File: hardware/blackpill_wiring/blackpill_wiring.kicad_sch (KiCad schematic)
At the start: 7 parts, among them J1 ST7789_DISPLAY, J2 HOBBY_SERVO, J3 CRSF_RECEIVER, J4 BRUSHLESS_ESC, J5 ESP01_WIFI, J6 USB_HOST, U1 BLACKPILL_F411CE

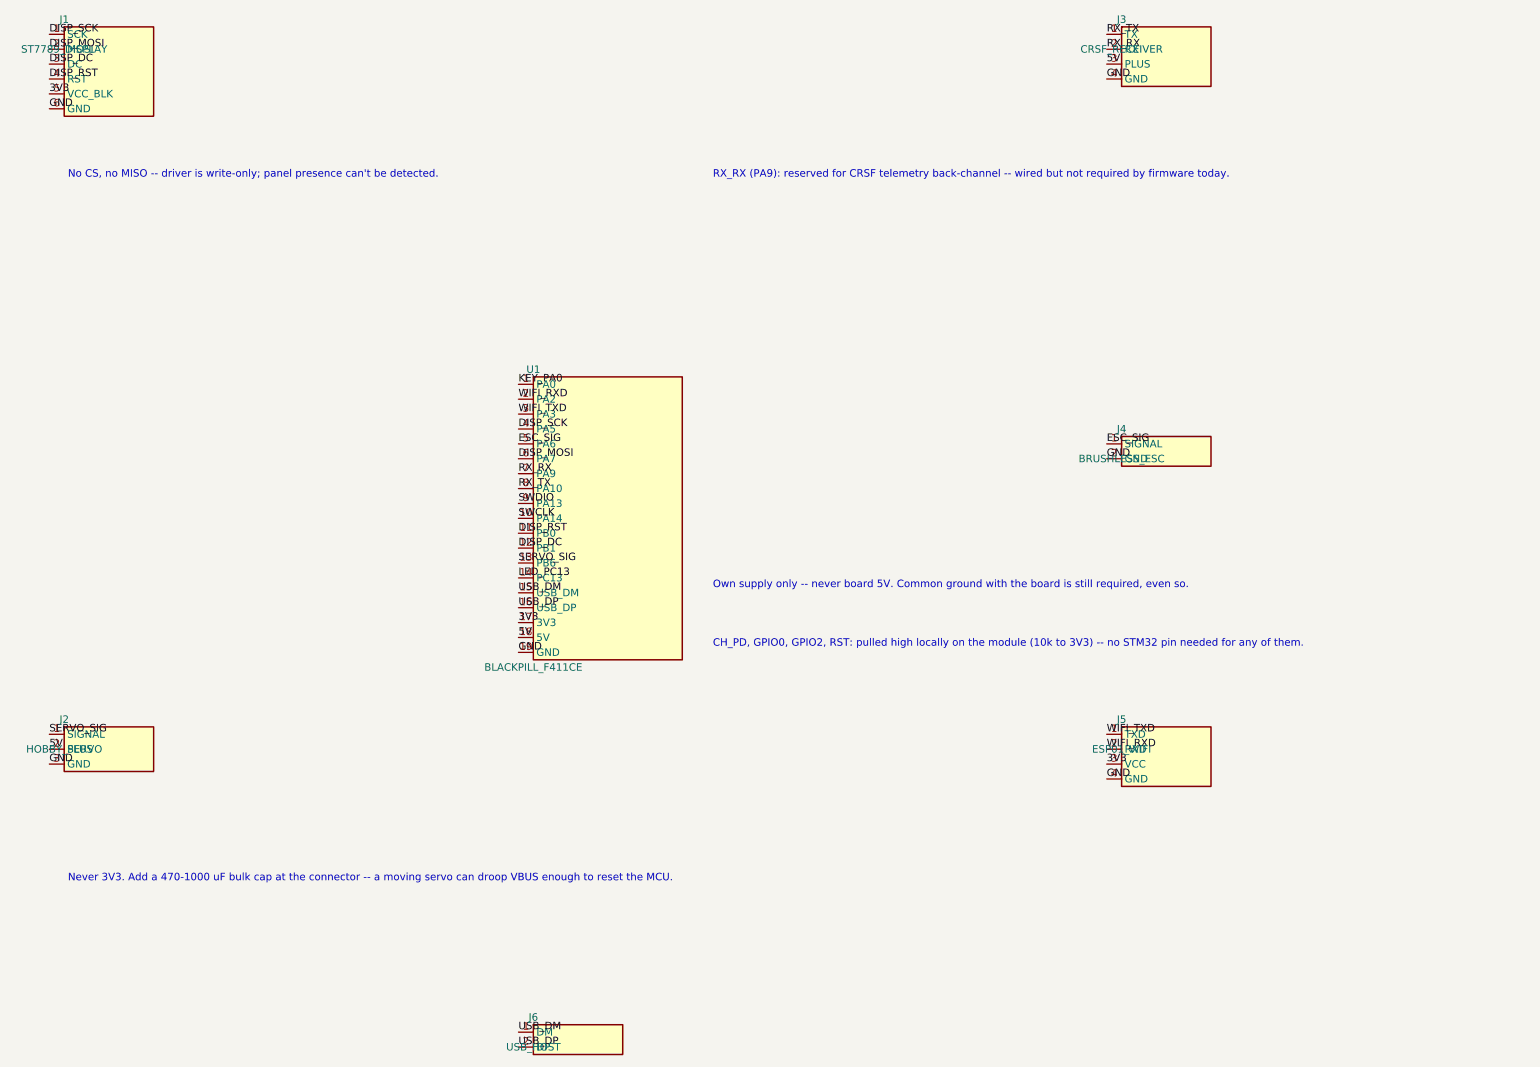
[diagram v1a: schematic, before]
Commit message: fix(hardware): draw real wires instead of net labels
Net labels were electrically correct (ERC-clean, all connections
verified) but visually unreadable as a wiring diagram: opening the
project showed components with no visible connection between them.
Reworked the schematic so every connection is an actual routed wire:

- BLACKPILL_F411CE now has pins split left/right (display+servo+USB
  on the left, receiver+ESC+WiFi on the right), matching the original
  SVG's own left/right stub grouping.
- ST7789_DISPLAY, HOBBY_SERVO and USB_HOST got their pins flipped to
  the right edge (facing the Black Pill, which sits to their right);
  CRSF_RECEIVER, BRUSHLESS_ESC and ESP01_WIFI keep their original
  left-facing pins (Black Pill sits to their right already).
- Every module's local pin Y-offsets are designed to exactly match
  the Black Pill's corresponding pin, then placed at the same sheet Y
  -- every wire is a straight 2-point horizontal line, no waypoint
  routing, no crossing over component bodies.
- Dropped PC13/PA0/PA13/PA14 as symbol pins entirely; the source SVG
  draws these as plain text badges, not wired stubs, so they're now
  add_schematic_text notes near U1 instead. Removes the 4 "label
  connected to only one pin" ERC notices from the previous version.

Verified against real KiCad 10.0.5 directly (not just the MCP
server's own tools, one of which -- list_schematic_nets -- turned out
to give a false "no nets found" on this file): `kicad-cli sch export
netlist` shows all 21 point-to-point nets correctly connected, and
`kicad-cli sch erc` reports 0 errors / 21 warnings, all either the
harmless lib_symbol_mismatch cache nag seen before or a cosmetic
endpoint_off_grid notice that doesn't affect actual connectivity.

Co-Authored-By: Claude Sonnet 5 <noreply@anthropic.com>
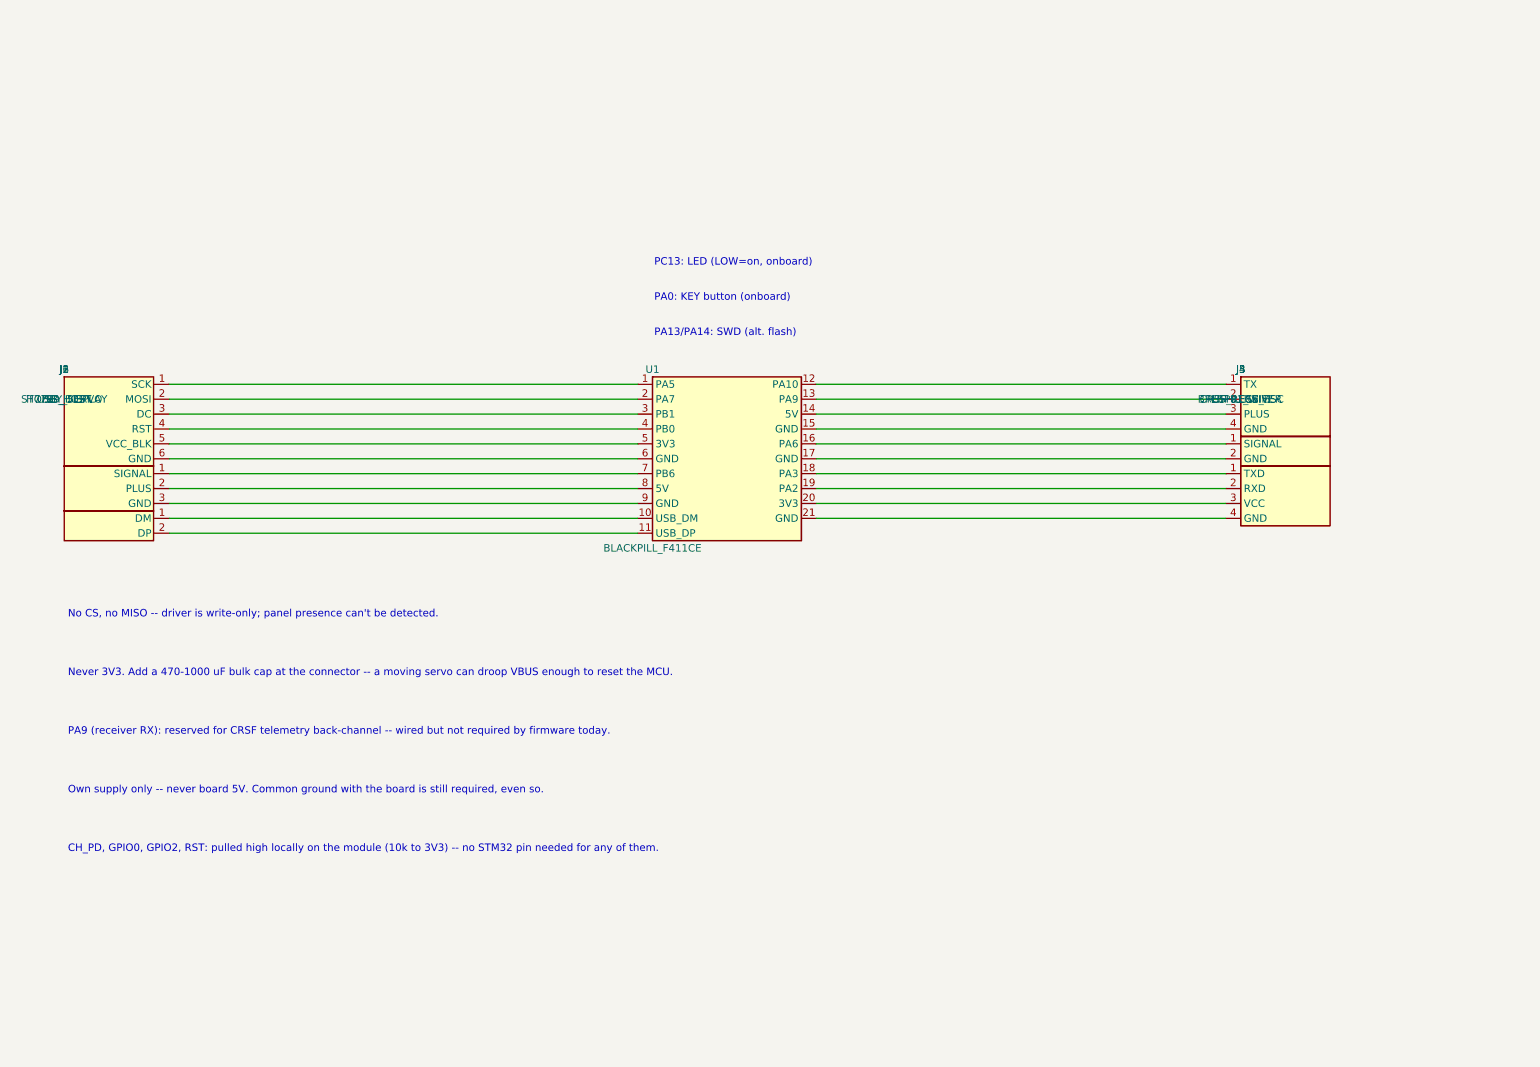
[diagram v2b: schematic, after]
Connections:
- net KEY_PA0 is gone; now on an unnamed net: U1.1 (PA5)
- removed net 3V3: J1.5 (VCC_BLK), J5.3 (VCC), U1.17 (3V3)
- removed net 5V: J2.2 (PLUS), J3.3 (PLUS), U1.18 (5V)
- net DISP_DC: no longer names the net of U1.12 (PA10)
- net DISP_DC: now also J3.1 (TX); no longer J1.3 (DC)
- net DISP_MOSI: no longer names the net of J1.2 (MOSI)
- net DISP_MOSI: now also U1.2 (PA7); no longer U1.6 (PA7)
- net DISP_RST: no longer names the net of U1.11 (USB_DP)
- net DISP_RST: now also J6.2 (DP); no longer J1.4 (RST)
- net DISP_SCK: no longer names the net of J1.1 (SCK)
- net DISP_SCK: no longer U1.4 (PA5)
- net ESC_SIG: no longer names the net of J4.1 (SIGNAL)
- net ESC_SIG: now also U1.16 (PA6); no longer U1.5 (PA6)
- removed net GND: J1.6 (GND), J2.3 (GND), J3.4 (GND), J4.2 (GND), J5.4 (GND), U1.19 (GND)
- net LED_PC13: no longer names the net of U1.14 (5V)
- net LED_PC13: now also J3.3 (PLUS)
- net RX_RX: no longer names the net of J3.2 (RX)
- net RX_RX: now also U1.13 (PA9); no longer U1.7 (PA9)
- net RX_TX: no longer names the net of U1.8 (5V)
- net RX_TX: now also J2.2 (PLUS); no longer J3.1 (TX)
- net SERVO_SIG: no longer names the net of J2.1 (SIGNAL)
- net SERVO_SIG: now also U1.7 (PB6); no longer U1.13 (PB6)
- net SWCLK: no longer names the net of U1.10 (USB_DM)
- net SWCLK: now also J6.1 (DM)
- net SWDIO: no longer names the net of U1.9 (GND)
- net SWDIO: now also J2.3 (GND)
- net USB_DM: no longer names the net of U1.15 (GND)
- net USB_DM: now also J3.4 (GND); no longer J6.1 (DM)
- removed net USB_DP: J6.2 (DP), U1.16 (USB_DP)
- net WIFI_RXD: no longer names the net of J5.2 (RXD)
- net WIFI_RXD: now also U1.19 (PA2); no longer U1.2 (PA2)
- net WIFI_TXD: no longer names the net of J5.1 (TXD)
- net WIFI_TXD: now also U1.18 (PA3); no longer U1.3 (PA3)
- new net: J4.2 (GND), U1.17 (GND)
- new net: J5.3 (VCC), U1.20 (3V3)
- new net: J5.4 (GND), U1.21 (GND)
- new net: J1.3 (DC), U1.3 (PB1)
- new net: J1.4 (RST), U1.4 (PB0)
- new net: J1.5 (VCC_BLK), U1.5 (3V3)
- new net: J1.6 (GND), U1.6 (GND)
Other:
- note added: "PA0: KEY button (onboard)"
- note added: "PA13/PA14: SWD (alt. flash)"
- note added: "PA9 (receiver RX): reserved for CRSF telemetry back-channel -- wired but not required by firmware today."
- note added: "PC13: LED (LOW=on, onboard)"
- note removed: "RX_RX (PA9): reserved for CRSF telemetry back-channel -- wired but not required by firmware today."
